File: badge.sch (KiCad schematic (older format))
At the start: 38 parts, among them J1 DevKitC_L, J10 HT024SQV003NH, J2 DevKitC_R, J3 HT024SQV010NH, J4 EXT1_1, J5 EXT1_2, J6 EXT1_3, J7 EXT2_1, J8 EXT2_2, J9 EXT2_3, SW1 UP, SW2 LEFT, SW3 A, SW4 DOWN, SW5 RIGHT, SW6 B, U1 ESP32-DEVKITC-32D

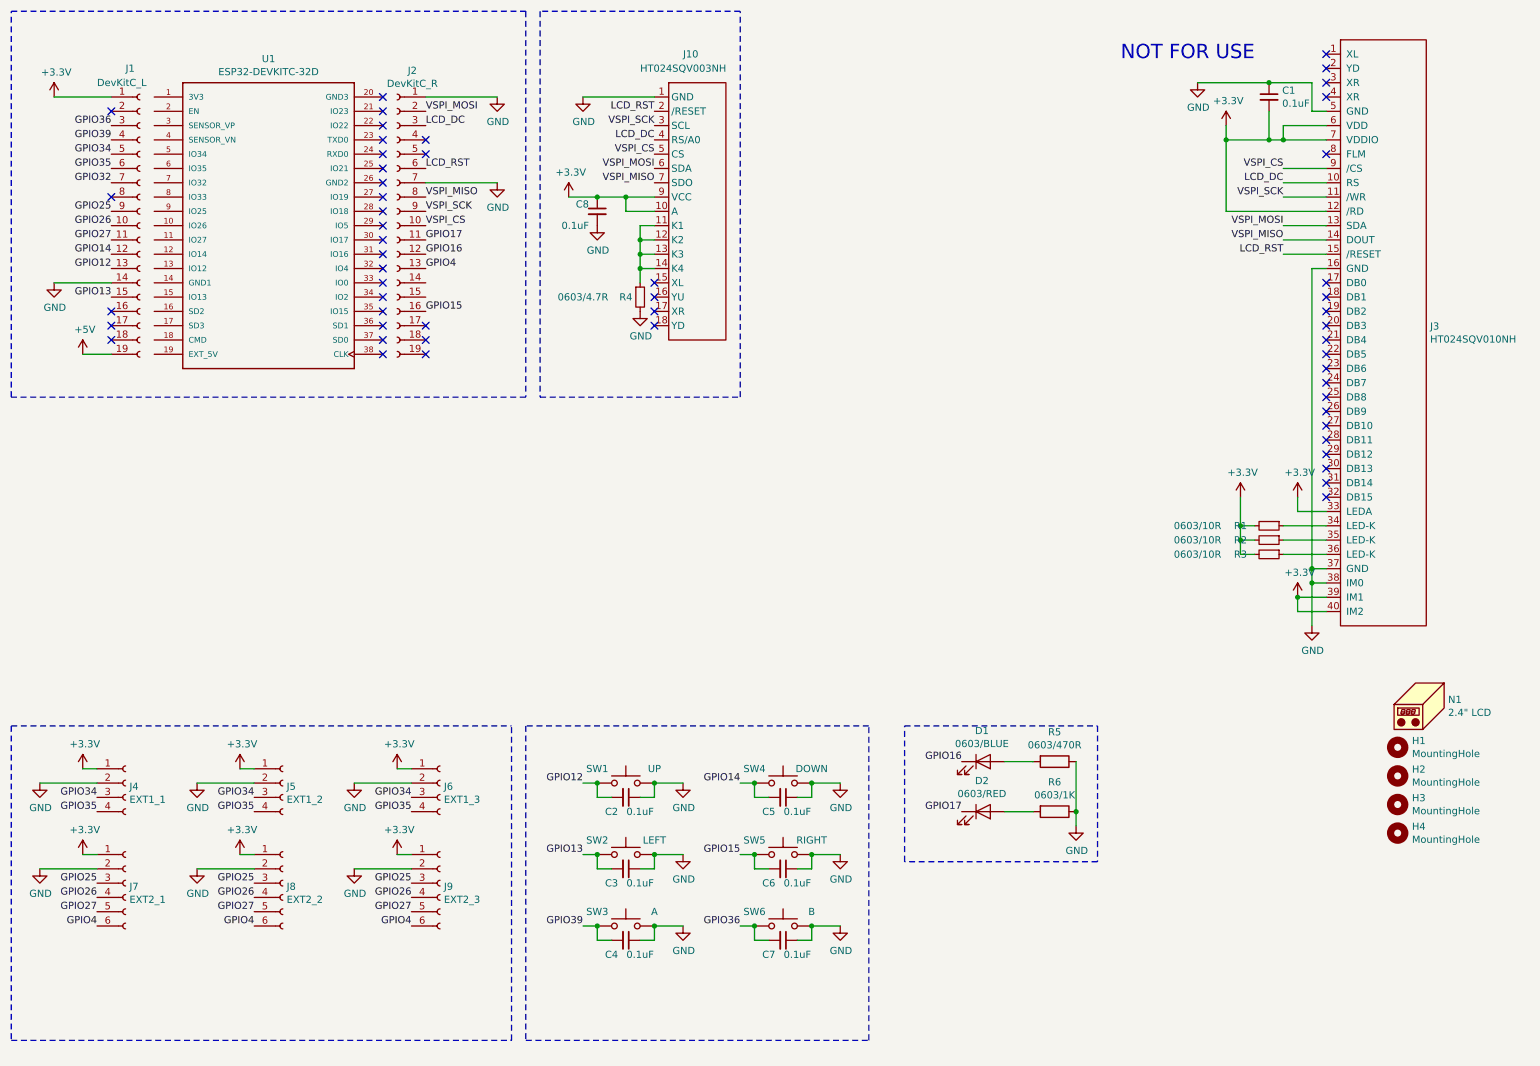
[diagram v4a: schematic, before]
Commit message: v0.2 add dust sensor and 5 way tact switch
* LED direction corrected
* Pin adjusted
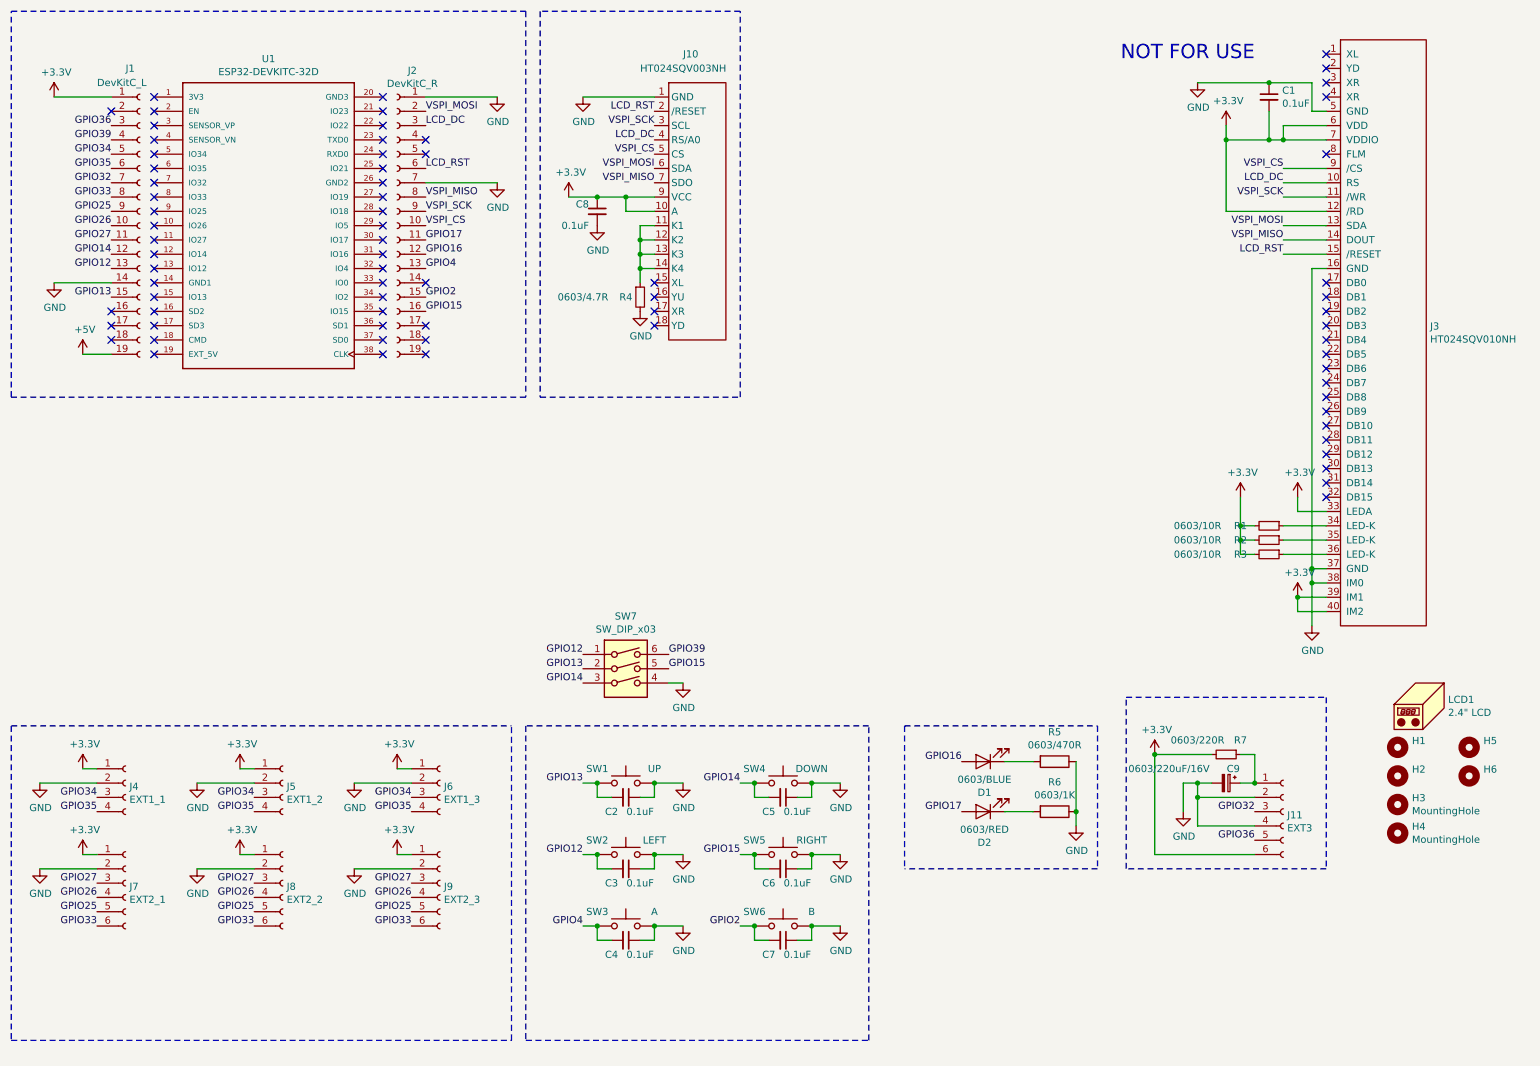
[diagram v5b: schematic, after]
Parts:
- added C9: 0603/220uF/16V, Capacitor_SMD:C_0603_1608Metric, symbol Device:CP_Small
- added H5, H6: MountingHole, custom_footprint:LanyardHole_6mm, symbol Mechanical:MountingHole
- added J11: EXT3, custom_footprint:PinSocket_1x06_P2.54mm_Vertical_NO3D, symbol Connector:Conn_01x06_Female
- added R7: 0603/220R, Resistor_SMD:R_0603_1608Metric, symbol Device:R_Small
- added SW7: SW_DIP_x03, custom_footprint:ITS-1500S, symbol Switch:SW_DIP_x03
- H1, H2: footprint MountingHole:MountingHole_5mm -> custom_footprint:LanyardHole_6mm
- renumbered N1 to LCD1
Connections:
- net +3V3: now also J11.6 (Pin_6), R7.2
- net GND: now also C9.2, J11.2 (Pin_2), J11.4 (Pin_4), SW7.4
- net GPIO12: now also C3.2, SW2.1, SW7.1; no longer C2.2, SW1.1
- net GPIO13: now also C2.2, SW1.1, SW7.2; no longer C3.2, SW2.1
- net GPIO14: now also SW7.3
- net GPIO15: now also SW7.5
- net GPIO16: now also D1.2 (A); no longer D1.1 (K)
- net GPIO17: now also D2.2 (A); no longer D2.1 (K)
- net GPIO25: now also J7.5 (Pin_5), J8.5 (Pin_5), J9.5 (Pin_5); no longer J7.3 (Pin_3), J8.3 (Pin_3), J9.3 (Pin_3)
- net GPIO27: now also J7.3 (Pin_3), J8.3 (Pin_3), J9.3 (Pin_3); no longer J7.5 (Pin_5), J8.5 (Pin_5), J9.5 (Pin_5)
- net GPIO32: now also J11.3 (Pin_3)
- net GPIO36: now also J11.5 (Pin_5); no longer C7.2, SW6.1
- net GPIO39: now also SW7.6; no longer C4.2, SW3.1
- net GPIO4: now also C4.2, SW3.1; no longer J7.6 (Pin_6), J8.6 (Pin_6), J9.6 (Pin_6)
- net GPIO33: now reaches J1.8 (Pin_8)
- net GPIO33: now also J7.6 (Pin_6), J8.6 (Pin_6), J9.6 (Pin_6)
- net GPIO2: now reaches J2.15 (Pin_15)
- net GPIO2: now also C7.2, SW6.1
- net at R5.2: now also D1.1 (K); no longer D1.2 (A)
- net at R6.2: now also D2.1 (K); no longer D2.2 (A)
- new net: C9.1, J11.1 (Pin_1), R7.1
- no-connect marks 54 -> 73
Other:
- moved on the sheet: D1, D2
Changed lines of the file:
@@
 Wire Wire Line
 	700  6500 1100 6500
-Text Label 1100 6600 2    50   ~ 0
+Text Label 1100 6900 2    50   ~ 0
+GPIO33
+Text Label 1100 6800 2    50   ~ 0
 GPIO25
 Text Label 1100 6700 2    50   ~ 0
 GPIO26
-Text Label 1100 6800 2    50   ~ 0
+Text Label 1100 6600 2    50   ~ 0
 GPIO27
-Text Label 1100 6900 2    50   ~ 0
-GPIO4
 Text Label 1200 1900 2    50   ~ 0
 GPIO25
@@
 	1    0    0    -1
 $EndComp
-Wire Wire Line
-	1800 6500 2200 6500
-Text Label 2200 6600 2    50   ~ 0
-GPIO25
-Text Label 2200 6700 2    50   ~ 0
-GPIO26
-Text Label 2200 6800 2    50   ~ 0
-GPIO27
-Text Label 2200 6900 2    50   ~ 0
-GPIO4
 $Comp
 L Connector:Conn_01x04_Female J6
@@
 Wire Wire Line
 	2900 6500 3300 6500
-Text Label 3300 6600 2    50   ~ 0
-GPIO25
-Text Label 3300 6700 2    50   ~ 0
-GPIO26
-Text Label 3300 6800 2    50   ~ 0
-GPIO27
-Text Label 3300 6900 2    50   ~ 0
-GPIO4
-NoConn ~ 1200 1800
 $Comp
 L power:+3.3V #PWR08
@@
 	4600 6000 4600 5900
 Text Label 4500 5900 2    50   ~ 0
-GPIO12
+GPIO13
 Wire Wire Line
 	4500 5900 4600 5900
@@
 	4600 6500 4600 6400
 Text Label 4500 6400 2    50   ~ 0
-GPIO13
+GPIO12
 Wire Wire Line
 	4500 6400 4600 6400
@@
 	4600 7000 4600 6900
 Text Label 4500 6900 2    50   ~ 0
-GPIO39
+GPIO4
 Wire Wire Line
 	4500 6900 4600 6900
@@
 	5700 7000 5700 6900
 Text Label 5600 6900 2    50   ~ 0
-GPIO36
+GPIO2
 Wire Wire Line
 	5600 6900 5700 6900
@@
 	6100 7000 6100 6900
 Connection ~ 6100 6900
-Text Label 1200 1300 2    50   ~ 0
-GPIO36
-Text Label 1200 1400 2    50   ~ 0
-GPIO39
 Text Label 1200 2300 2    50   ~ 0
 GPIO12
@@
 P 10200 5650
 F 0 "H1" H 10300 5696 50  0000 L CNN
-F 1 "MountingHole" H 10300 5605 50  0000 L CNN
-F 2 "MountingHole:MountingHole_5mm" H 10200 5650 50  0001 C CNN
+F 1 "MountingHole" H 10300 5605 50  0001 L CNN
+F 2 "custom_footprint:LanyardHole_6mm" H 10200 5650 50  0001 C CNN
 F 3 "~" H 10200 5650 50  0001 C CNN
 	1    10200 5650
@@
 P 10200 5850
 F 0 "H2" H 10300 5896 50  0000 L CNN
-F 1 "MountingHole" H 10300 5805 50  0000 L CNN
-F 2 "MountingHole:MountingHole_5mm" H 10200 5850 50  0001 C CNN
+F 1 "MountingHole" H 10300 5805 50  0001 L CNN
+F 2 "custom_footprint:LanyardHole_6mm" H 10200 5850 50  0001 C CNN
 F 3 "~" H 10200 5850 50  0001 C CNN
 	1    10200 5850
@@
 $EndComp
 $Comp
-L Mechanical:Housing N1
+L Mechanical:Housing LCD1
 U 1 1 5BE12A6D
 P 10400 5350
-F 0 "N1" H 10553 5384 50  0000 L CNN
+F 0 "LCD1" H 10553 5384 50  0000 L CNN
 F 1 "2.4\" LCD" H 10553 5293 50  0000 L CNN
 F 2 "custom_footprint:2.4INCH_TFT_LCD_18P_0.80mm_FOLD" H 10450 5400 50  0001 C CNN
@@
 NoConn ~ 3100 1900
 NoConn ~ 3100 2000
-NoConn ~ 3100 2100
-NoConn ~ 3100 2200
-NoConn ~ 3100 2300
 NoConn ~ 3100 2400
-NoConn ~ 3100 2500
-NoConn ~ 3100 2600
 NoConn ~ 3100 2700
 NoConn ~ 3100 2800
@@
 F 3 "~" H 7300 5750 50  0001 C CNN
 	1    7300 5750
-	1    0    0    -1
+	-1   0    0    1
 $EndComp
 $Comp
@@
 F 3 "~" H 7300 6100 50  0001 C CNN
 	1    7300 6100
-	1    0    0    -1
+	-1   0    0    1
 $EndComp
 $Comp
@@
 	6750 5500 8100 5500
 Wire Notes Line
-	8100 5500 8100 6450
-Wire Notes Line
-	8100 6450 6750 6450
-Wire Notes Line
-	6750 6450 6750 5500
+	8100 6500 6750 6500
 $Comp
 L Mechanical:MountingHole H3
@@
 Text Notes 9200 850  2    100  ~ 0
 NOT FOR USE
+$Comp
+L Mechanical:MountingHole H5
+U 1 1 5BEB88E9
+P 10700 5650
+F 0 "H5" H 10800 5696 50  0000 L CNN
+F 1 "MountingHole" H 10800 5605 50  0001 L CNN
+F 2 "custom_footprint:LanyardHole_6mm" H 10700 5650 50  0001 C CNN
+F 3 "~" H 10700 5650 50  0001 C CNN
+	1    10700 5650
+	1    0    0    -1
+$EndComp
+$Comp
+L Mechanical:MountingHole H6
+U 1 1 5BEB88EF
+P 10700 5850
+F 0 "H6" H 10800 5896 50  0000 L CNN
+F 1 "MountingHole" H 10800 5805 50  0001 L CNN
+F 2 "custom_footprint:LanyardHole_6mm" H 10700 5850 50  0001 C CNN
+F 3 "~" H 10700 5850 50  0001 C CNN
+	1    10700 5850
+	1    0    0    -1
+$EndComp
+$Comp
+L Connector:Conn_01x06_Female J11
+U 1 1 5BEBD3AB
+P 9400 6100
+F 0 "J11" H 9427 6076 50  0000 L CNN
+F 1 "EXT3" H 9427 5985 50  0000 L CNN
+F 2 "custom_footprint:PinSocket_1x06_P2.54mm_Vertical_NO3D" H 9400 6100 50  0001 C CNN
+F 3 "~" H 9400 6100 50  0001 C CNN
+	1    9400 6100
+	1    0    0    -1
+$EndComp
+$Comp
+L power:+3.3V #PWR0115
+U 1 1 5BEBD6A8
+P 8500 5700
+F 0 "#PWR0115" H 8500 5550 50  0001 C CNN
+F 1 "+3.3V" H 8515 5873 50  0000 C CNN
+F 2 "" H 8500 5700 50  0001 C CNN
+F 3 "" H 8500 5700 50  0001 C CNN
+	1    8500 5700
+	1    0    0    -1
+$EndComp
+Wire Wire Line
+	8500 6400 9200 6400
+Text Label 1200 1800 2    50   ~ 0
+GPIO33
+Text Label 3400 2500 0    50   ~ 0
+GPIO2
+NoConn ~ 3100 2100
+NoConn ~ 3100 2200
+NoConn ~ 3100 2600
+NoConn ~ 3100 2500
+NoConn ~ 3100 2300
+NoConn ~ 3400 2400
+NoConn ~ 1500 1100
+NoConn ~ 1500 1200
+NoConn ~ 1500 1300
+NoConn ~ 1500 1400
+NoConn ~ 1500 1500
+NoConn ~ 1500 1600
+NoConn ~ 1500 1700
+NoConn ~ 1500 1800
+NoConn ~ 1500 1900
+NoConn ~ 1500 2000
+NoConn ~ 1500 2100
+NoConn ~ 1500 2200
+NoConn ~ 1500 2300
+NoConn ~ 1500 2400
+NoConn ~ 1500 2500
+NoConn ~ 1500 2600
+NoConn ~ 1500 2700
+NoConn ~ 1500 2800
+NoConn ~ 1500 2900
+Text Label 1200 1300 2    50   ~ 0
+GPIO36
+Wire Wire Line
+	1800 6500 2200 6500
+Text Label 2200 6900 2    50   ~ 0
+GPIO33
+Text Label 2200 6800 2    50   ~ 0
+GPIO25
+Text Label 2200 6700 2    50   ~ 0
+GPIO26
+Text Label 2200 6600 2    50   ~ 0
+GPIO27
+Text Label 3300 6900 2    50   ~ 0
+GPIO33
+Text Label 3300 6800 2    50   ~ 0
+GPIO25
+Text Label 3300 6700 2    50   ~ 0
+GPIO26
+Text Label 3300 6600 2    50   ~ 0
+GPIO27
+Text Label 9200 6300 2    50   ~ 0
+GPIO36
+Text Label 9200 6100 2    50   ~ 0
+GPIO32
+$Comp
+L power:GND #PWR021
+U 1 1 5BF5B4B6
+P 8700 6100
+F 0 "#PWR021" H 8700 5850 50  0001 C CNN
+F 1 "GND" H 8705 5927 50  0000 C CNN
+F 2 "" H 8700 6100 50  0001 C CNN
+F 3 "" H 8700 6100 50  0001 C CNN
+	1    8700 6100
+	1    0    0    -1
+$EndComp
+Wire Wire Line
+	9200 6000 8800 6000
+Wire Wire Line
+	8800 6000 8800 6200
+Wire Wire Line
+	8800 6200 9200 6200
+Connection ~ 8800 6000
+$Comp
+L Device:R_Small R7
+U 1 1 5BF6463D
+P 9000 5700
+F 0 "R7" V 8900 5800 50  0000 C CNN
+F 1 "0603/220R" V 8900 5500 50  0000 C CNN
+F 2 "Resistor_SMD:R_0603_1608Metric" H 9000 5700 50  0001 C CNN
+F 3 "~" H 9000 5700 50  0001 C CNN
+	1    9000 5700
+	0    1    1    0
+$EndComp
+Wire Wire Line
+	9100 5900 9200 5900
+$Comp
+L Device:CP_Small C9
+U 1 1 5BF69367
+P 9000 5900
+F 0 "C9" V 8900 5950 50  0000 C CNN
+F 1 "0603/220uF/16V" V 8900 5500 50  0000 C CNN
+F 2 "Capacitor_SMD:C_0603_1608Metric" H 9000 5900 50  0001 C CNN
+F 3 "~" H 9000 5900 50  0001 C CNN
+	1    9000 5900
+	0    1    1    0
+$EndComp
+Wire Wire Line
+	9200 5900 9200 5700
+Connection ~ 9200 5900
+Wire Wire Line
+	8900 5700 8500 5700
+Connection ~ 8500 5700
+Wire Notes Line
+	8300 5300 9700 5300
+Wire Notes Line
+	9700 5300 9700 6500
+Wire Notes Line
+	9700 6500 8300 6500
+Wire Notes Line
+	8300 6500 8300 5300
+Wire Notes Line
+	8100 5500 8100 6500
+Wire Notes Line
+	6750 5500 6750 6500
+Wire Wire Line
+	9100 5700 9200 5700
+Wire Wire Line
+	8500 5700 8500 6400
+Wire Wire Line
+	8900 5900 8800 5900
+Wire Wire Line
+	8800 5900 8800 6000
+Wire Wire Line
+	8800 5900 8700 5900
+Wire Wire Line
+	8700 5900 8700 6100
+Connection ~ 8800 5900
+$Comp
+L Switch:SW_DIP_x03 SW7
+U 1 1 5C00FC92
+P 4800 5200
+F 0 "SW7" H 4800 5667 50  0000 C CNN
+F 1 "SW_DIP_x03" H 4800 5576 50  0000 C CNN
+F 2 "custom_footprint:ITS-1500S" H 4800 5200 50  0001 C CNN
+F 3 "" H 4800 5200 50  0001 C CNN
+	1    4800 5200
+	1    0    0    -1
+$EndComp
+$Comp
+L power:GND #PWR0116
+U 1 1 5C00FD62
+P 5200 5200
+F 0 "#PWR0116" H 5200 4950 50  0001 C CNN
+F 1 "GND" H 5205 5027 50  0000 C CNN
+F 2 "" H 5200 5200 50  0001 C CNN
+F 3 "" H 5200 5200 50  0001 C CNN
+	1    5200 5200
+	1    0    0    -1
+$EndComp
+Wire Wire Line
+	5100 5200 5200 5200
+Text Label 4500 5000 2    50   ~ 0
+GPIO12
+Text Label 4500 5100 2    50   ~ 0
+GPIO13
+Text Label 4500 5200 2    50   ~ 0
+GPIO14
+Text Label 5100 5100 0    50   ~ 0
+GPIO15
+Text Label 1200 1400 2    50   ~ 0
+GPIO39
+Text Label 5100 5000 0    50   ~ 0
+GPIO39
 $EndSCHEMATC

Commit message: v0.3 0.3mm track, SMT/THT pinsocket support
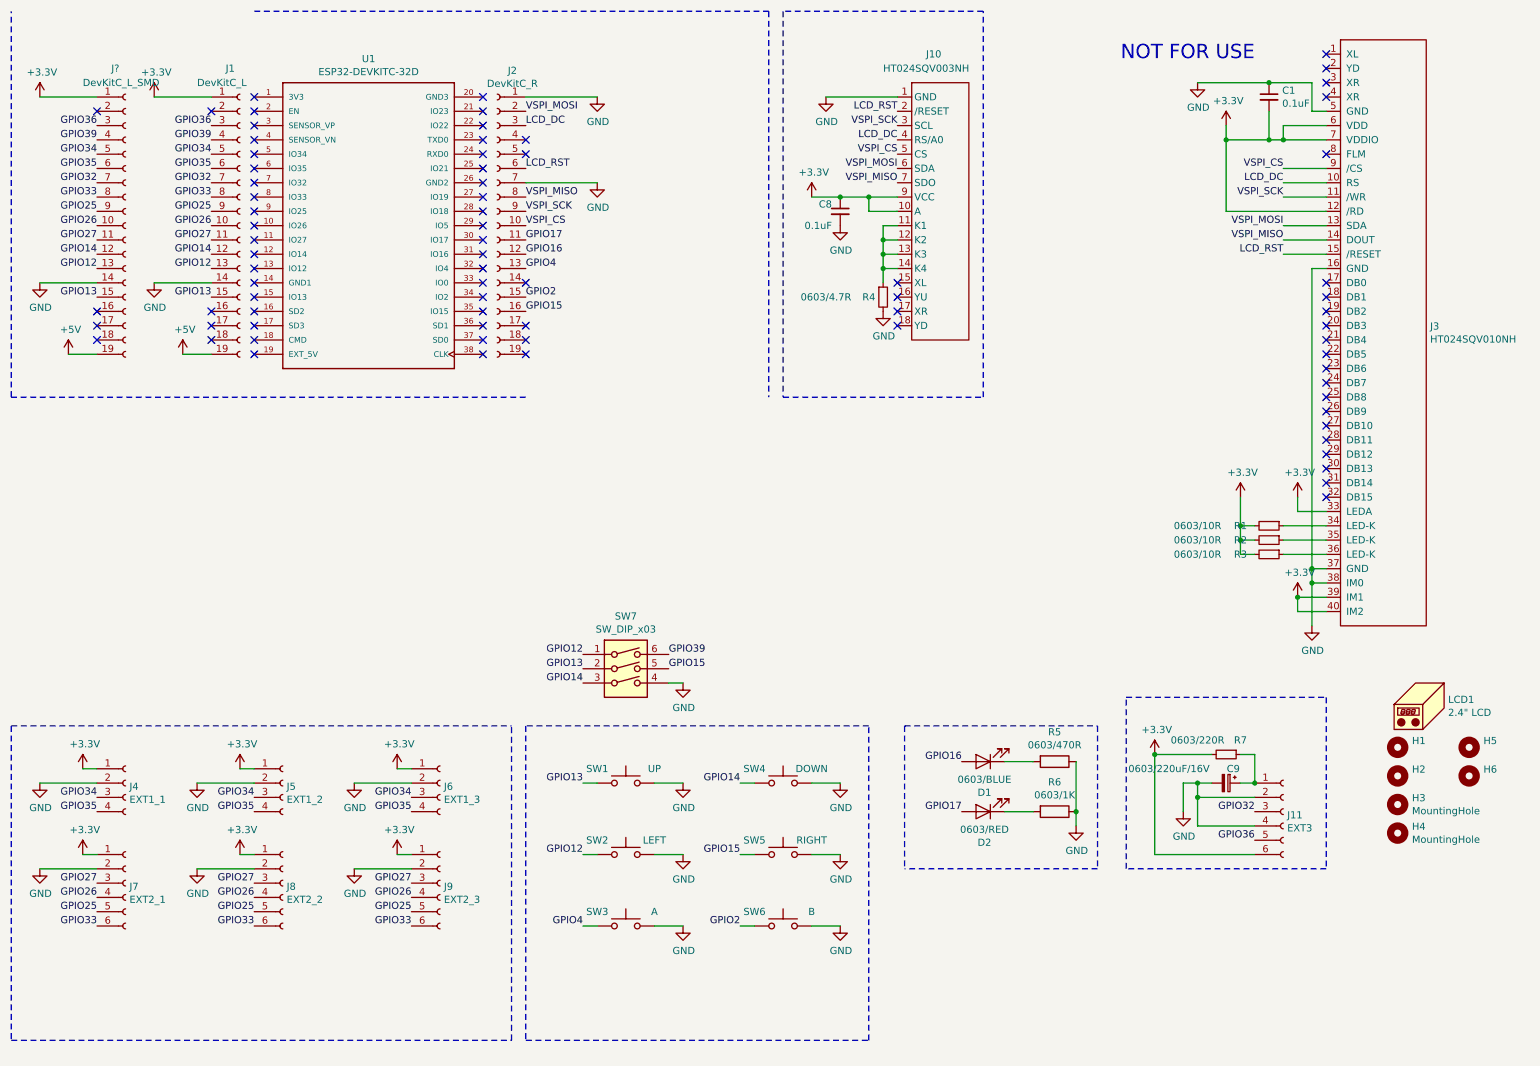
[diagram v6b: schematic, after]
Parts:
- removed C2, C3, C4, C5, C6, C7: 0.1uF, Capacitor_SMD:C_0603_1608Metric, symbol Device:C_Small
- added J?: DevKitC_L_SMD, Connector_PinSocket_2.54mm:PinSocket_1x19_P2.54mm_Vertical_SMD_Pin1Right, symbol Connector:Conn_01x19_Female
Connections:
- net +3V3: now also J?.1 (Pin_1)
- net +5V: now also J?.19 (Pin_19)
- net GND: now also J?.14 (Pin_14)
- net GPIO12: now also J?.13 (Pin_13)
- net GPIO13: now also J?.15 (Pin_15)
- net GPIO14: now also J?.12 (Pin_12)
- net GPIO25: now also J?.9 (Pin_9)
- net GPIO26: now also J?.10 (Pin_10)
- net GPIO27: now also J?.11 (Pin_11)
- net GPIO32: now also J?.7 (Pin_7)
- net GPIO33: now also J?.8 (Pin_8)
- net GPIO34: now also J?.5 (Pin_5)
- net GPIO35: now also J?.6 (Pin_6)
- net GPIO36: now also J?.3 (Pin_3)
- net GPIO39: now also J?.4 (Pin_4)
- no-connect marks 73 -> 77
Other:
- moved on the sheet: C8, J1, J10, J2, R4, U1
